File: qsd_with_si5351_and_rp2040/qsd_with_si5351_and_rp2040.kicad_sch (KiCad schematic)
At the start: 59 parts, among them U3 LM4562, U4 LM4562, U5 LM4562

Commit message: schematic ~ done - try some layout
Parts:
- removed C?: 1n, Capacitor_SMD:C_0805_2012Metric, symbol Device:C_Small
- added H1, H2, H3, H4: M3, MountingHole:MountingHole_3.2mm_M3_DIN965_Pad_TopBottom, symbol Mechanical:MountingHole
- added J3: Conn_01x04, Connector_PinHeader_2.54mm:PinHeader_1x04_P2.54mm_Vertical, symbol Connector_Generic:Conn_01x04
- added J?: SSM-120-F-DV, Connector_PinSocket_2.54mm:PinSocket_2x20_P2.54mm_Vertical_SMD, symbol Connector_Generic:Conn_02x20_Odd_Even
- FB1, FB3, FB4, FB5, FB6: renamed from FB?; value 1000ohms -> 1000; footprint Resistor_SMD:R_0805_2012Metric_Pad1.20x1.40mm_HandSolder -> Inductor_SMD:L_0805_2012Metric_Pad1.05x1.20mm_HandSolder
- FB2: renamed from FB?; value 1000ohms -> 1000; footprint (none) -> Inductor_SMD:L_0805_2012Metric_Pad1.05x1.20mm_HandSolder
- J1: renamed from J?; footprint (none) -> parts:60312202114508
- J2: renamed from J?; footprint (none) -> Connector_USB:USB_C_Receptacle_GCT_USB4105-xx-A_16P_TopMnt_Horizontal
- R19, R20: value 1000 -> 2.2k
- R24, R25: value 10k -> 2.2k
- U1: renamed from U?; footprint (none) -> parts:CX2047LNL
- U3, U4, U5: footprint (none) -> Package_SO:SO-8_3.9x4.9mm_P1.27mm
- gave numbers to parts that had none: 13
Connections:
- net GND: now also J3.2 (Pin_2), J3.3 (Pin_3), J?.15 (Pin_15), J?.16 (Pin_16), J?.5 (Pin_5), J?.6 (Pin_6)
- net OUT_I: now also J3.1 (Pin_1); no longer C17.2
- net VCC_3V3 renamed VCC_3V3_MIX
- new net 3V3_EN: J?.8 (Pin_8)
- new net 3V3_OUT: J?.10 (Pin_10)
- new net ADC_VREF: J?.12 (Pin_12)
- new net GPIO0: J?.1 (Pin_1)
- new net GPIO1: J?.3 (Pin_3)
- new net GPIO10: J?.27 (Pin_27)
- new net GPIO11: J?.29 (Pin_29)
- new net GPIO12: J?.31 (Pin_31)
- new net GPIO13: J?.33 (Pin_33)
- new net GPIO14: J?.37 (Pin_37)
- new net GPIO15: J?.39 (Pin_39)
- new net GPIO16: J?.40 (Pin_40)
- new net GPIO17: J?.38 (Pin_38)
- new net GPIO18: J?.34 (Pin_34)
- new net GPIO19: J?.32 (Pin_32)
- new net GPIO2: J?.7 (Pin_7)
- new net GPIO20: J?.30 (Pin_30)
- new net GPIO21: J?.28 (Pin_28)
- new net GPIO22: J?.24 (Pin_24)
- new net GPIO23: J?.26 (Pin_26)
- new net GPIO24: J?.36 (Pin_36)
- new net GPIO25: J?.35 (Pin_35)
- new net GPIO26: J?.20 (Pin_20)
- new net GPIO27: J?.18 (Pin_18)
- new net GPIO28: J?.14 (Pin_14)
- new net GPIO29: J?.25 (Pin_25)
- new net GPIO3: J?.9 (Pin_9)
- new net GPIO4: J?.11 (Pin_11)
- new net GPIO5: J?.13 (Pin_13)
- new net GPIO6: J?.17 (Pin_17)
- new net GPIO7: J?.19 (Pin_19)
- new net GPIO8: J?.21 (Pin_21)
- new net GPIO9: J?.23 (Pin_23)
- new net OUT_Q: C17.2, J3.4 (Pin_4)
- new net RUN: J?.22 (Pin_22)
- new net VBUS: J?.2 (Pin_2)
- new net VDD_SYS: J?.4 (Pin_4)
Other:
- added sheet power (power.kicad_sch)
- note added: "SSM-120-F-DV SOCKET M20-8762042 HEADER"
- moved on the sheet: C1, C10, C11, C12, C13, C14, C15, C17, C2, C3, C4, C5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

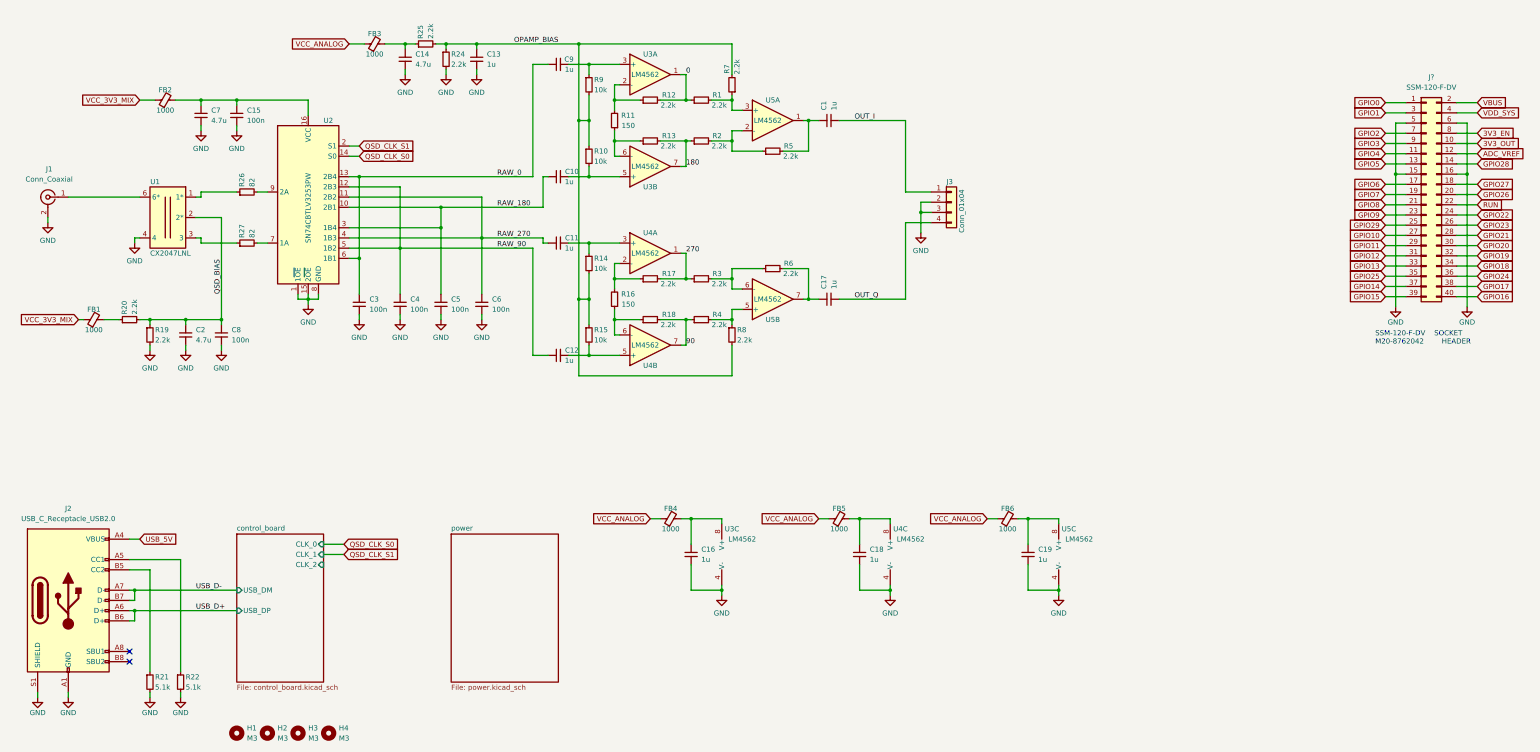
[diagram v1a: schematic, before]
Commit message: version with stackable connector
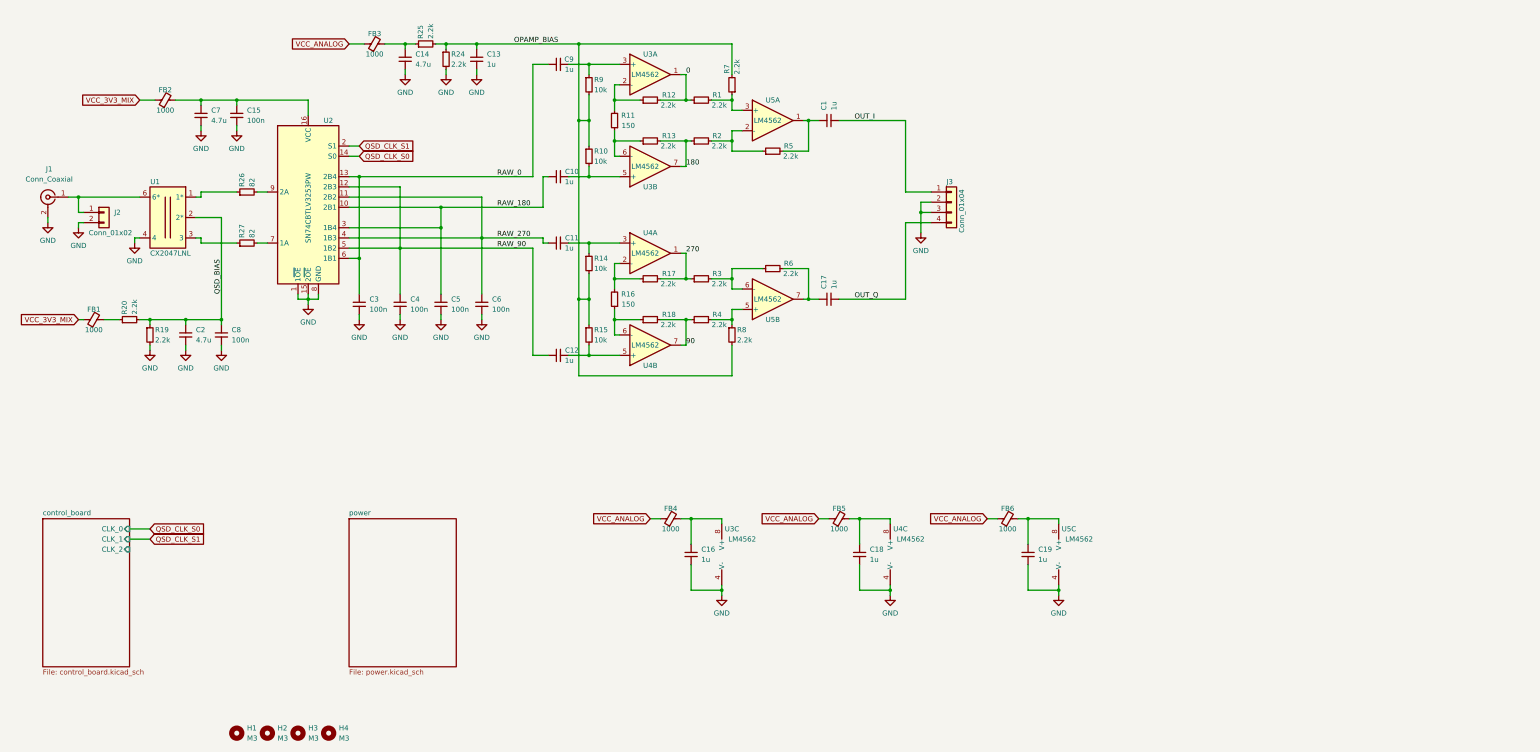
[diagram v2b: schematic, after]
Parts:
- removed J2: USB_C_Receptacle_USB2.0, Connector_USB:USB_C_Receptacle_GCT_USB4105-xx-A_16P_TopMnt_Horizontal, symbol Connector:USB_C_Receptacle_USB2.0
- removed J?: SSM-120-F-DV, Connector_PinSocket_2.54mm:PinSocket_2x20_P2.54mm_Vertical_SMD, symbol Connector_Generic:Conn_02x20_Odd_Even
- removed R21, R22: 5.1k, Resistor_SMD:R_0805_2012Metric_Pad1.20x1.40mm_HandSolder, symbol Device:R_Small
- added J2: Conn_01x02, Connector_PinHeader_2.54mm:PinHeader_1x02_P2.54mm_Vertical, symbol Connector_Generic:Conn_01x02
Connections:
- net GND: now also J2.2 (Pin_2)
- net at J1.1 (In), U1.6 (6*): now also J2.1 (Pin_1)
- no-connect marks 2 -> 0
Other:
- sheet control_board ports: added none; removed USB_DM, USB_DP
- note removed: "SSM-120-F-DV SOCKET M20-8762042 HEADER"
